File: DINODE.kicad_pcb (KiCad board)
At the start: 2 copper layers, 76.2 x 90.2 mm, 36 parts, among them J1 Barrel_Jack, J10 Conn_01x03_Male, J11 Conn_02x04_Odd_Even, J12 Conn_01x03_Female, J13 Conn_02x04_Odd_Even, J2 Conn_01x02_Male, J3 Conn_01x07, J4 Conn_01x16, J5 Conn_02x04_Odd_Even, J6 Conn_02x04_Odd_Even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

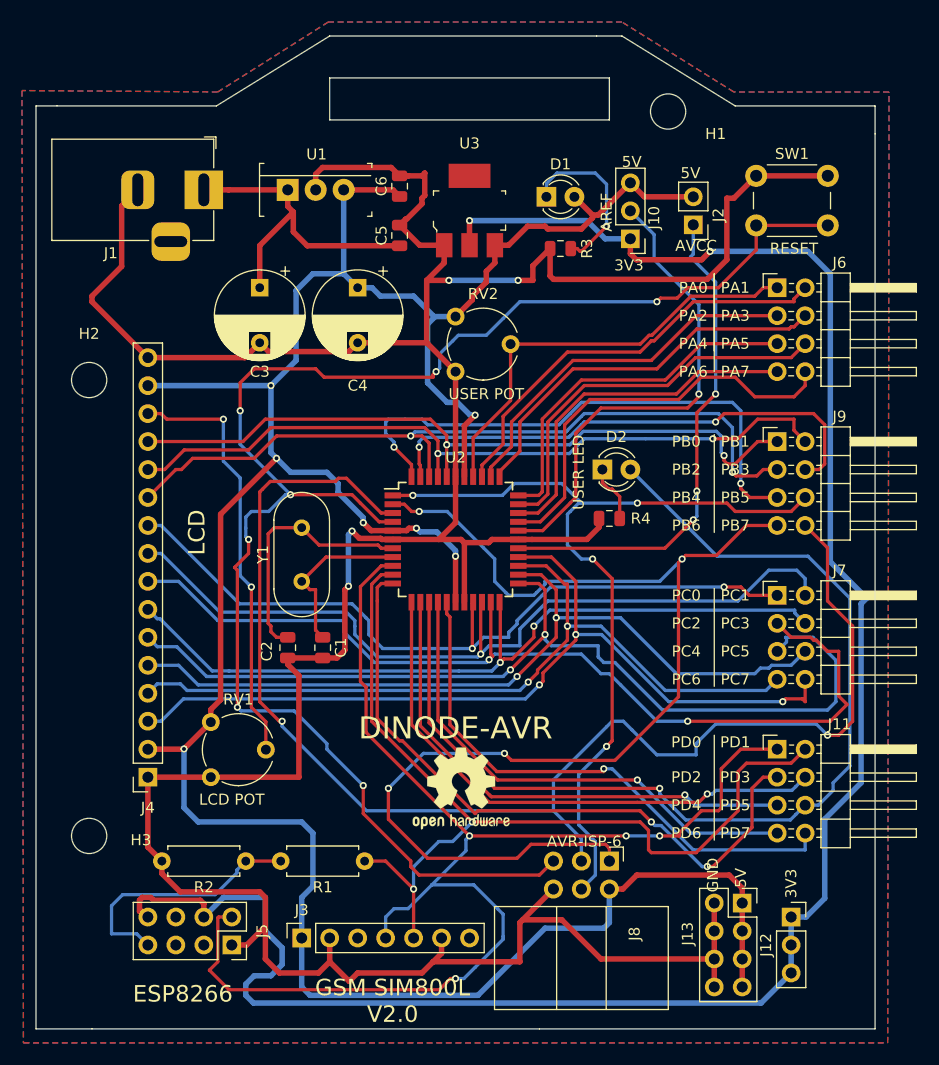
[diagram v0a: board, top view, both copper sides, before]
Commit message: updated edge cuts and copper fill zones
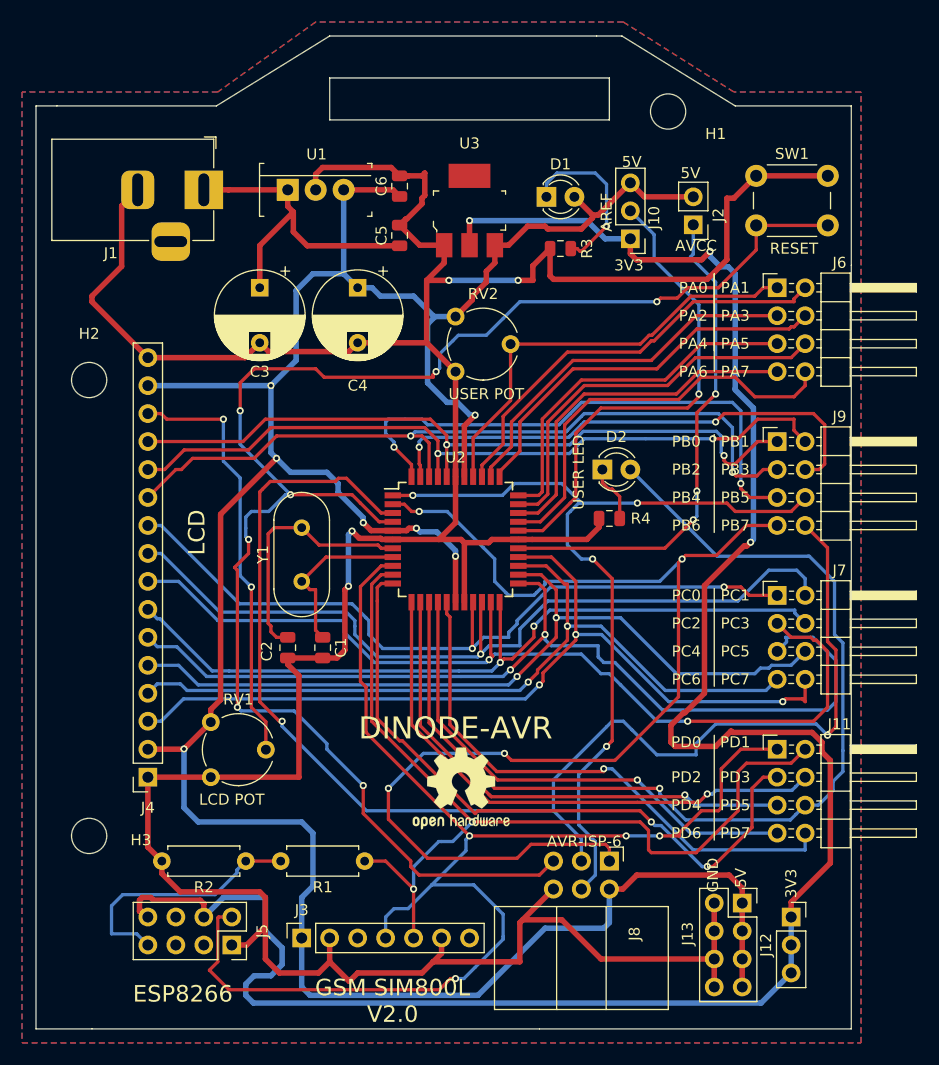
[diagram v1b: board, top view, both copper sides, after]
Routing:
- net +3V3: track 185.4 -> 192.7 mm, vias 2 -> 3
- net PC_2: track 87.8 -> 84.9 mm
- net PB_7: track 125.3 -> 123.5 mm
- net PD_5: track 95.6 -> 95.0 mm
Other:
- board size 76.2 x 90.2 mm -> 74 x 90.2 mm

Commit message: Added gerber files
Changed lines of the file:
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@@
 (kicad_pcb (version 20171130) (host pcbnew "(5.1.2)-2")
   (general
-    (thickness 1.6)
-    (drawings 72)
+    (thickness 1)
+    (drawings 82)
     (tracks 1033)
     (zones 0)
@@
       (usegerberextensions false)
       (usegerberattributes false)
-      (usegerberadvancedattributes false)
+      (usegerberadvancedattributes true)
       (creategerberjobfile false)
-      (excludeedgelayer true)
+      (excludeedgelayer false)
       (linewidth 0.100000)
       (plotframeref false)
@@
       (plotvalue true)
       (plotinvisibletext false)
-      (padsonsilk false)
+      (padsonsilk true)
       (subtractmaskfromsilk false)
       (outputformat 1)
       (mirror false)
-      (drillshape 1)
+      (drillshape 0)
       (scaleselection 1)
-      (outputdirectory ""))
+      (outputdirectory "plots/"))
   )
   (net 0 "")
@@
     (pad 1 np_thru_hole circle (at 0 0) (size 3.2 3.2) (drill 3.2) (layers *.Cu *.Mask))
   )
+  (gr_circle (center 117.475 79.375) (end 117.602 79.121) (layer F.SilkS) (width 0.12))
+  (dimension 6.35 (width 0.12) (layer F.SilkS)
+    (gr_text "6.350 mm" (at 171.45 42.545 270) (layer F.SilkS)
+      (effects (font (size 1 1) (thickness 0.15)))
+    )
+    (feature1 (pts (xy 159.131 45.72) (xy 170.766421 45.72)))
+    (feature2 (pts (xy 159.131 39.37) (xy 170.766421 39.37)))
+    (crossbar (pts (xy 170.18 39.37) (xy 170.18 45.72)))
+    (arrow1a (pts (xy 170.18 45.72) (xy 169.593579 44.593496)))
+    (arrow1b (pts (xy 170.18 45.72) (xy 170.766421 44.593496)))
+    (arrow2a (pts (xy 170.18 39.37) (xy 169.593579 40.496504)))
+    (arrow2b (pts (xy 170.18 39.37) (xy 170.766421 40.496504)))
+  )
+  (dimension 83.82 (width 0.12) (layer F.SilkS)
+    (gr_text "83.820 mm" (at 178.943 87.63 90) (layer F.SilkS)
+      (effects (font (size 1 1) (thickness 0.15)))
+    )
+    (feature1 (pts (xy 159.131 45.72) (xy 178.259421 45.72)))
+    (feature2 (pts (xy 159.131 129.54) (xy 178.259421 129.54)))
+    (crossbar (pts (xy 177.673 129.54) (xy 177.673 45.72)))
+    (arrow1a (pts (xy 177.673 45.72) (xy 178.259421 46.846504)))
+    (arrow1b (pts (xy 177.673 45.72) (xy 177.086579 46.846504)))
+    (arrow2a (pts (xy 177.673 129.54) (xy 178.259421 128.413496)))
+    (arrow2b (pts (xy 177.673 129.54) (xy 177.086579 128.413496)))
+  )
+  (dimension 10.541 (width 0.12) (layer F.SilkS)
+    (gr_text "10.541 mm" (at 153.8605 42.291) (layer F.SilkS)
+      (effects (font (size 1 1) (thickness 0.15)))
+    )
+    (feature1 (pts (xy 159.131 45.72) (xy 159.131 42.974579)))
+    (feature2 (pts (xy 148.59 45.72) (xy 148.59 42.974579)))
+    (crossbar (pts (xy 148.59 43.561) (xy 159.131 43.561)))
+    (arrow1a (pts (xy 159.131 43.561) (xy 158.004496 44.147421)))
+    (arrow1b (pts (xy 159.131 43.561) (xy 158.004496 42.974579)))
+    (arrow2a (pts (xy 148.59 43.561) (xy 149.716504 44.147421)))
+    (arrow2b (pts (xy 148.59 43.561) (xy 149.716504 42.974579)))
+  )
+  (dimension 12.089039 (width 0.12) (layer F.SilkS)
+    (gr_text "12.089 mm" (at 145.839676 38.668055 328.3136323) (layer F.SilkS)
+      (effects (font (size 1 1) (thickness 0.15)))
+    )
+    (feature1 (pts (xy 148.59 45.72) (xy 150.624113 42.424737)))
+    (feature2 (pts (xy 138.303 39.37) (xy 140.337113 36.074737)))
+    (crossbar (pts (xy 140.029084 36.573744) (xy 150.316084 42.923744)))
+    (arrow1a (pts (xy 150.316084 42.923744) (xy 149.049473 42.831033)))
+    (arrow1b (pts (xy 150.316084 42.923744) (xy 149.66553 41.83302)))
+    (arrow2a (pts (xy 140.029084 36.573744) (xy 140.679638 37.664468)))
+    (arrow2b (pts (xy 140.029084 36.573744) (xy 141.295695 36.666455)))
+  )
+  (dimension 26.543 (width 0.12) (layer F.SilkS)
+    (gr_text "26.543 mm" (at 125.0315 36.195) (layer F.SilkS)
+      (effects (font (size 1 1) (thickness 0.15)))
+    )
+    (feature1 (pts (xy 138.303 39.37) (xy 138.303 36.878579)))
+    (feature2 (pts (xy 111.76 39.37) (xy 111.76 36.878579)))
+    (crossbar (pts (xy 111.76 37.465) (xy 138.303 37.465)))
+    (arrow1a (pts (xy 138.303 37.465) (xy 137.176496 38.051421)))
+    (arrow1b (pts (xy 138.303 37.465) (xy 137.176496 36.878579)))
+    (arrow2a (pts (xy 111.76 37.465) (xy 112.886504 38.051421)))
+    (arrow2b (pts (xy 111.76 37.465) (xy 112.886504 36.878579)))
+  )
+  (dimension 12.089039 (width 0.12) (layer F.SilkS)
+    (gr_text "12.089 mm" (at 104.54219 39.184618 31.68636769) (layer F.SilkS)
+      (effects (font (size 1 1) (thickness 0.15)))
+    )
+    (feature1 (pts (xy 111.76 39.37) (xy 110.044754 36.591301)))
+    (feature2 (pts (xy 101.473 45.72) (xy 99.757754 42.941301)))
+    (crossbar (pts (xy 100.065782 43.440307) (xy 110.352782 37.090307)))
+    (arrow1a (pts (xy 110.352782 37.090307) (xy 109.702228 38.181031)))
+    (arrow1b (pts (xy 110.352782 37.090307) (xy 109.086171 37.183018)))
+    (arrow2a (pts (xy 100.065782 43.440307) (xy 101.332393 43.347596)))
+    (arrow2b (pts (xy 100.065782 43.440307) (xy 100.716336 42.349583)))
+  )
+  (dimension 16.383 (width 0.12) (layer F.SilkS)
+    (gr_text "16.383 mm" (at 93.2815 42.672) (layer F.SilkS)
+      (effects (font (size 1 1) (thickness 0.15)))
+    )
+    (feature1 (pts (xy 101.473 45.72) (xy 101.473 43.355579)))
+    (feature2 (pts (xy 85.09 45.72) (xy 85.09 43.355579)))
+    (crossbar (pts (xy 85.09 43.942) (xy 101.473 43.942)))
+    (arrow1a (pts (xy 101.473 43.942) (xy 100.346496 44.528421)))
+    (arrow1b (pts (xy 101.473 43.942) (xy 100.346496 43.355579)))
+    (arrow2a (pts (xy 85.09 43.942) (xy 86.216504 44.528421)))
+    (arrow2b (pts (xy 85.09 43.942) (xy 86.216504 43.355579)))
+  )
+  (dimension 83.82 (width 0.12) (layer F.SilkS)
+    (gr_text "83.820 mm" (at 81.534 87.63 270) (layer F.SilkS)
+      (effects (font (size 1 1) (thickness 0.15)))
+    )
+    (feature1 (pts (xy 85.09 129.54) (xy 82.217579 129.54)))
+    (feature2 (pts (xy 85.09 45.72) (xy 82.217579 45.72)))
+    (crossbar (pts (xy 82.804 45.72) (xy 82.804 129.54)))
+    (arrow1a (pts (xy 82.804 129.54) (xy 82.217579 128.413496)))
+    (arrow1b (pts (xy 82.804 129.54) (xy 83.390421 128.413496)))
+    (arrow2a (pts (xy 82.804 45.72) (xy 82.217579 46.846504)))
+    (arrow2b (pts (xy 82.804 45.72) (xy 83.390421 46.846504)))
+  )
+  (dimension 74.041 (width 0.12) (layer F.SilkS)
+    (gr_text "74.041 mm" (at 122.1105 133.730999) (layer F.SilkS)
+      (effects (font (size 1 1) (thickness 0.15)))
+    )
+    (feature1 (pts (xy 159.131 129.54) (xy 159.131 133.04742)))
+    (feature2 (pts (xy 85.09 129.54) (xy 85.09 133.04742)))
+    (crossbar (pts (xy 85.09 132.460999) (xy 159.131 132.460999)))
+    (arrow1a (pts (xy 159.131 132.460999) (xy 158.004496 133.04742)))
+    (arrow1b (pts (xy 159.131 132.460999) (xy 158.004496 131.874578)))
+    (arrow2a (pts (xy 85.09 132.460999) (xy 86.216504 133.04742)))
+    (arrow2b (pts (xy 85.09 132.460999) (xy 86.216504 131.874578)))
+  )
   (gr_line (start 159.131 129.54) (end 130.81 129.54) (layer Edge.Cuts) (width 0.05))

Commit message: updated gerber files
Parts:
- moved REF** 1.05 mm to (122.7, 107.4)
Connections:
- J4 pad 10: PC_0 -> PD_6
- J4 pad 9: PC_1 -> PD_7
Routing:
- net PC_1: track 75.1 -> 40.1 mm
- net PC_0: track 69.8 -> 35.0 mm
- net PD_6: track 45.8 -> 78.6 mm, vias 1 -> 2
- net PD_7: track 50.1 -> 82.5 mm, vias 1 -> 2
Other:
- board text added: "jackagwaya@gmail.com"
